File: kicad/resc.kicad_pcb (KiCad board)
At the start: 4 copper layers, 51 x 75 mm, 164 parts, among them J1 CAN, J10 Conn_Coaxial, J2 HALL, J3 COMM, J4 POWER BTN, J5 SERVO, J6 SWD, J7 LED1, J8 LED2, J9 USB_C_Receptacle_USB2.0_14P, Q1 IRF7749L1, Q2 IRF7749L1, Q3 IRF7749L1, Q4 IRF7749L1, Q5 IRF7749L1, Q6 IRF7749L1, Q7 DMN62D0UW-7, SW1 SENSOR_VOLTAGE, U1 STM32F405RGTx, U10 AD8418, U11 SN74LVC1G66DCKR, U12 SN74LVC1G66DCKR, U13 SN74LVC1G66DCKR, U14 TC2117-3.3VDBTR, U15 USBLC6-2SC6, U16 NRF52832-QFAA-R, U2 TJA1051T-3, U3 SN74LVC1G66DCKR, U5 SN74LVC1G66DCKR, U6 SN74LVC1G66DCKR, U7 BMI160, U8 AD8418, U9 AD8418, Y1 8MHz, Y2 32MHz

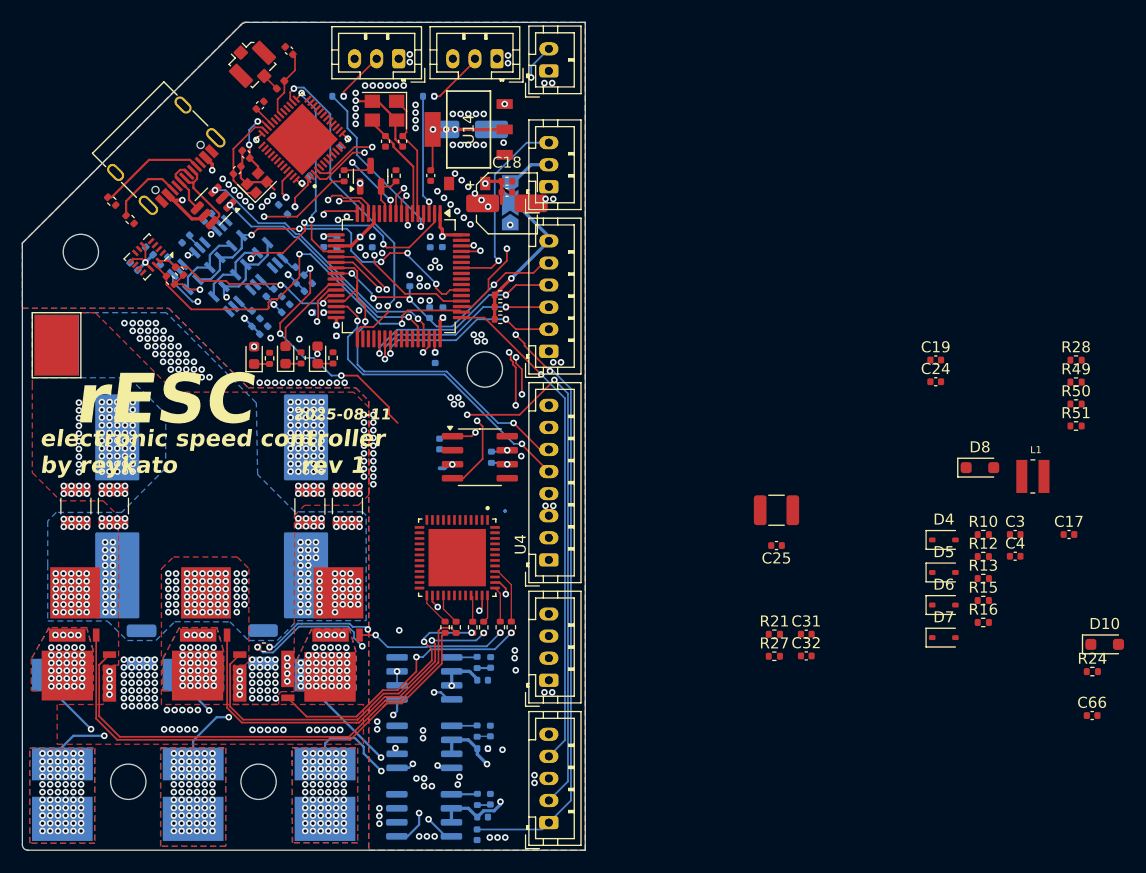
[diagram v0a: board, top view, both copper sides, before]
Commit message: revision 2 is complete, sent to manufacturer
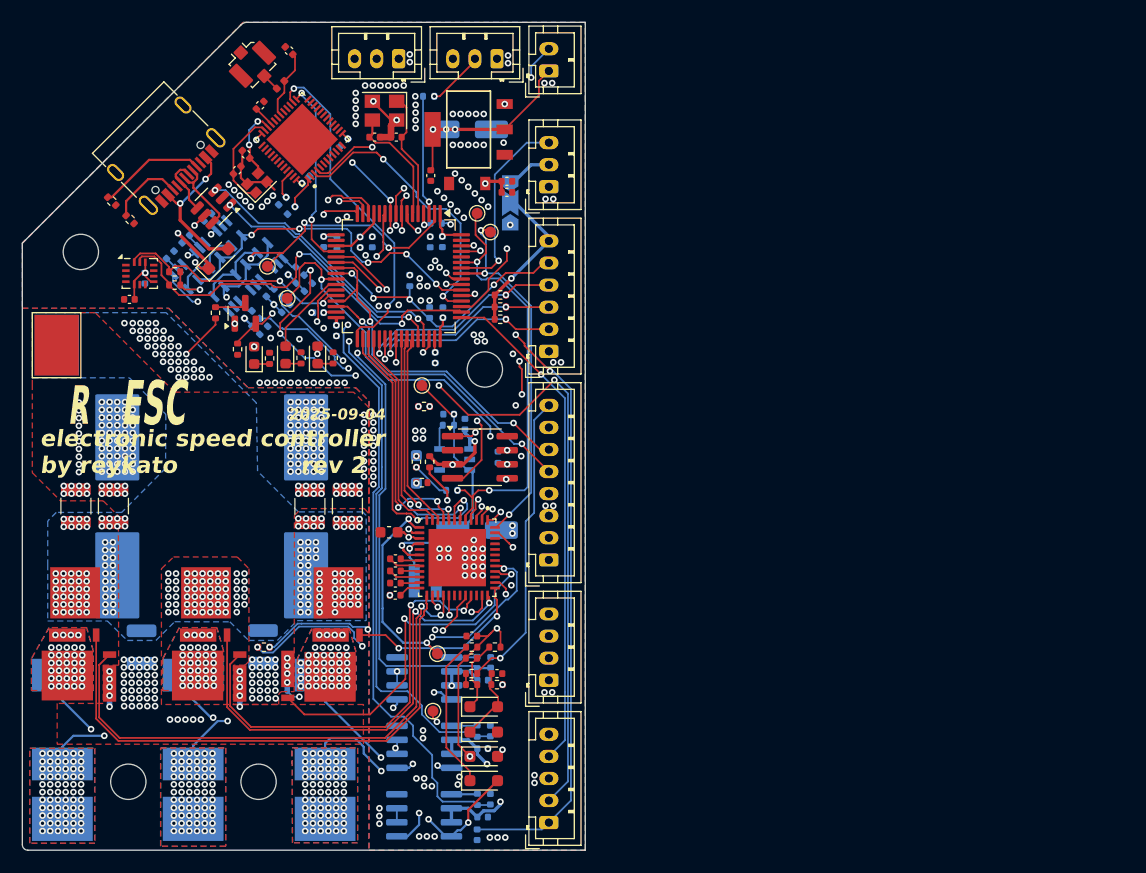
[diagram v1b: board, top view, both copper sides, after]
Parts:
- removed C23: 4.7uF 100V, Capacitor_SMD:C_1210_3225Metric
- removed C31: 120pF, Capacitor_SMD:C_0402_1005Metric
- removed C32: 6.8nF, Capacitor_SMD:C_0402_1005Metric
- removed R27: 15k, Resistor_SMD:R_0402_1005Metric
- removed R28: 10k, Resistor_SMD:R_0402_1005Metric
- removed R31, R32, R33, R37, R38, R39: 4.7R, Resistor_SMD:R_0402_1005Metric
- added C21: 100nF 63V, Capacitor_SMD:C_0603_1608Metric, F.Cu at (153.2, 91.2)
- added NT1: NetTie_2, NetTie:NetTie-2_SMD_Pad0.5mm, B.Cu at (144.0, 105.2)
- added NT2: NetTie_2, NetTie:NetTie-2_SMD_Pad0.5mm, B.Cu at (139.7, 106.5)
- added NT3: NetTie_2, NetTie:NetTie-2_SMD_Pad0.5mm, B.Cu at (127.9, 106.5)
- added R22: 0R, Resistor_SMD:R_0402_1005Metric, B.Cu at (158.6, 81.5)
- added R25: 0R, Resistor_SMD:R_0402_1005Metric, F.Cu at (156.9, 84.8)
- added TP1: DRV_CE, TestPoint:TestPoint_Pad_D1.0mm, F.Cu at (157.2, 107.4)
- added TP10: nFAULT, TestPoint:TestPoint_Pad_D1.0mm, F.Cu at (161.2, 62.3)
- added TP11: EN_GATE, TestPoint:TestPoint_Pad_D1.0mm, F.Cu at (162.4, 64.0)
- added TP12: nBRAKE, TestPoint:TestPoint_Pad_D1.0mm, F.Cu at (157.6, 102.2)
- added TP2: SENS_FILT, TestPoint:TestPoint_Pad_D1.0mm, F.Cu at (142.2, 67.1)
- added TP8: BUCK_V, TestPoint:TestPoint_Pad_D1.0mm, F.Cu at (156.2, 77.9)
- added TP9: SHUTDOWN, TestPoint:TestPoint_Pad_D1.0mm, F.Cu at (144.0, 70.0)
- added U17: ~, footprints:SOT-23-5-DBV_TEX, B.Cu at (159.2, 84.6)
- C17, C18, C66, D8, L1, R49: moved to B.Cu
- C20, C36: moved to F.Cu
- D4, D5, D6, D7: footprint Diode_SMD:D_SOD-323 -> Diode_SMD:D_SOD-323_HandSoldering
- moved D10 87.6 mm to (137.8, 66.4), turned to 45 degrees
- moved C66 64.4 mm to (158.6, 80.5), turned to 180 degrees
- moved R51 59.8 mm to (155.7, 84.8), turned to 90 degrees
- moved R50 59.1 mm to (156.4, 79.8), turned to 180 degrees
- moved R49 57.4 mm to (158.9, 87.4)
- moved L1 55.9 mm to (156.5, 95.6), turned to 180 degrees
- moved C17 55.6 mm to (160.1, 81.4), turned to 90 degrees
- moved R24 54.2 mm to (162.8, 101.6)
- moved C19 53.4 mm to (153.8, 96.9), turned to 180 degrees
- moved C24 51.9 mm to (153.8, 94.7), turned to 180 degrees
- moved D8 51.1 mm to (155.7, 85.5), turned to 90 degrees
- moved C3 50.1 mm to (160.7, 100.6), turned to 180 degrees
- moved C4 48.1 mm to (163.0, 104.0)
- moved R10 47.5 mm to (160.7, 101.6), turned to 180 degrees
- moved R12 47.3 mm to (160.7, 102.6)
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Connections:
- net /Shunt Amplifiers/C_A renamed /MOSFETs/C_A
- net /Shunt Amplifiers/C_B renamed /MOSFETs/C_B
- net /Shunt Amplifiers/C_C renamed /MOSFETs/C_C
- net /Shunt Amplifiers/PH_A renamed /MOSFETs/PH_A
- net /Shunt Amplifiers/PH_B renamed /MOSFETs/PH_B
- net /Shunt Amplifiers/PH_C renamed /MOSFETs/PH_C
- C3 pad 1: /EN_BUCK -> /DRV_CE
- C66 pad 1: /Power/DRV_BUCK_OUT -> /Gate Driver/DRV_BUCK_OUT
- D6 pad 1: /EN_BUCK -> /DRV_CE
- J4 pad 1: GND -> VDD
- J9 pad A4: Net-(J9-VBUS-PadA4) -> Net-(D10-A)
- J9 pad A9: Net-(J9-VBUS-PadA4) -> Net-(D10-A)
- J9 pad B4: Net-(J9-VBUS-PadA4) -> Net-(D10-A)
- J9 pad B9: Net-(J9-VBUS-PadA4) -> Net-(D10-A)
- Q1 pad G: Net-(Q1-PadG) -> /Gate Driver/GH_A
- Q2 pad G: Net-(Q2-PadG) -> /Gate Driver/GH_B
- Q3 pad G: Net-(Q3-PadG) -> /Gate Driver/GH_C
- Q4 pad G: Net-(Q4-PadG) -> /Gate Driver/GL_A
- Q5 pad G: Net-(Q5-PadG) -> /Gate Driver/GL_B
- Q6 pad G: Net-(Q6-PadG) -> /Gate Driver/GL_C
- R10 pad 1: /EN_BUCK -> /DRV_CE
- R12 pad 1: /EN_BUCK -> /DRV_CE
- R24 pad 1: Net-(J9-VBUS-PadA4) -> Net-(D5-K)
- R24 pad 2: Net-(D10-A) -> /DRV_CE
- U1 pad 53: /MCU/SPI3_SCK -> /Gate Driver/SCK
- U1 pad 59: /MCU/FAULT -> /Gate Driver/nFAULT
- U4 pad 14: +5V -> Net-(U4-DVDD)
- U4 pad 29: GND -> /Gate Driver/SL_C
- U4 pad 32: GND -> /Gate Driver/SL_B
- U4 pad 41: GND -> /Gate Driver/SL_A
- U4 pad 47: /Gate Driver/DRV_CE -> /DRV_CE
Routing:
- net /MCU/CURRENT_1: track 29.6 -> 93.2 mm, vias 2 -> 4
- net /MCU/CURRENT_3: track 22.9 -> 81.4 mm, vias 3 -> 5
- net /SHUTDOWN: track 0.00 -> 55.6 mm, vias 0 -> 3
- net /MCU/CURRENT_2: track 27.8 -> 81.7 mm, vias 2 -> 4
- net /Gate Driver/GL_C: track 2.86 -> 50.1 mm, vias 0 -> 2
- net /Gate Driver/GH_C: track 3.05 -> 49.5 mm
- net /Gate Driver/SH_B: track 37.4 -> 83.4 mm, vias 37 -> 39
- net Net-(Q3-PadG): track 45.9 -> 0.00 mm
- net Net-(Q6-PadG): track 45.1 -> 0.00 mm
- net /Gate Driver/GH_B: track 2.52 -> 42.1 mm, vias 0 -> 2
- net /Gate Driver/nFAULT: track 0.00 -> 39.4 mm, vias 0 -> 3
- net /Gate Driver/SL_C: track 0.00 -> 37.5 mm, vias 0 -> 2
- net /Gate Driver/GL_B: track 2.44 -> 39.2 mm, vias 0 -> 2
- net /Gate Driver/SH_C: track 60.8 -> 96.3 mm, vias 37 -> 38
- net Net-(Q2-PadG): track 35.3 -> 0.00 mm, vias 2 -> 0
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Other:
- board text added: "2025-09-04"
- board text added: "ESC"
- board text added: "R"
- board text added: "rev 2"
- board text removed: "2025-08-11"
- board text removed: "rESC"
- board text removed: "rev 1"
